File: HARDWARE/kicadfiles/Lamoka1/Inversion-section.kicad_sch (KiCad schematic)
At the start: 30 parts, among them Q1 NMOS, Q2 NMOS, Q3 CSD19536KCS, Q4 CSD19536KCS, Q5 CSD19536KCS, Q6 CSD19536KCS, U4 LM5122MH/NOPB

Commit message: Finishing routing for H bridge (Inversion-section)
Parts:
- added C22, C23: C, symbol Device:C
- added D11, D12: D, symbol Device:D
- added R10, R12: R, SOIC_14L_TEX, symbol Device:R
- added R13, R14, R15, R16: 10k, symbol Device:R
- added R17, R18: R, symbol Device:R
- added U5, U6: UCC27735DR, SOIC_14L_TEX, symbol UCC27735DR:UCC27735DR
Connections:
- net 11-14v input: now also D11.2 (A), D12.2 (A), U5.4 (EN/NC), U5.7 (VDD), U6.4 (EN/NC), U6.7 (VDD)
- net G4S: now also C23.2, R14.1, U6.11 (HS)
- net GND: now also R15.1, R16.1, U5.3 (VSS), U5.5 (COM), U6.3 (VSS), U6.5 (COM)
- net Q3G: now also R13.2, R17.2
- net Q3S: now also C22.2, R13.1, U5.11 (HS)
- net Q4G: now also R14.2, R18.2
- net Q5G: now also R10.1, R15.2
- net Q6G: now also R12.1, R16.2
- new net GPIO1: U5.1 (HI)
- new net GPIO2: U5.2 (LI)
- new net GPIO3: U6.1 (HI)
- new net GPIO4: U6.2 (LI)
- new net HB1: C22.1, D11.1 (K), U5.13 (HB)
- new net HB2: C23.1, D12.1 (K), U6.13 (HB)
- new net HO1: R17.1, U5.12 (HO)
- new net HO2: R18.1, U6.12 (HO)
- new net LO1: R10.2, U5.6 (LO)
- new net LO2: R12.2, U6.6 (LO)
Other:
- note removed: "Need the H bridge setup here"

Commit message: ADD logo, repo grade, and cosmetic/finishing H bridge connections
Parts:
- added J1: Connect to transformer, Connector:Tag-Connect_TC2030-IDC-FP_2x03_P1.27mm_Vertical, symbol Connector:Conn_01x02_Pin
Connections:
- net G4S: now also J1.1 (Pin_1)
- net Q3S: now also J1.2 (Pin_2)
- net HO1: no longer names the net of R17.1, U5.12 (HO)
- net HO2: no longer names the net of R18.1, U6.12 (HO)
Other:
- note added: "H-Bridge-Sub-Section"
- note removed: "Then transformer here"
- moved on the sheet: C22, C23, D11, D12, Q3, Q4, Q5, Q6, R10, R12, R13, R14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

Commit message: Improving repository
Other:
- title: Inverting  -> Inversion-Section 
- moved on the sheet: C22, C23, D11, D12, J1, Q3, Q4, Q5, Q6, R10, R12, R13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

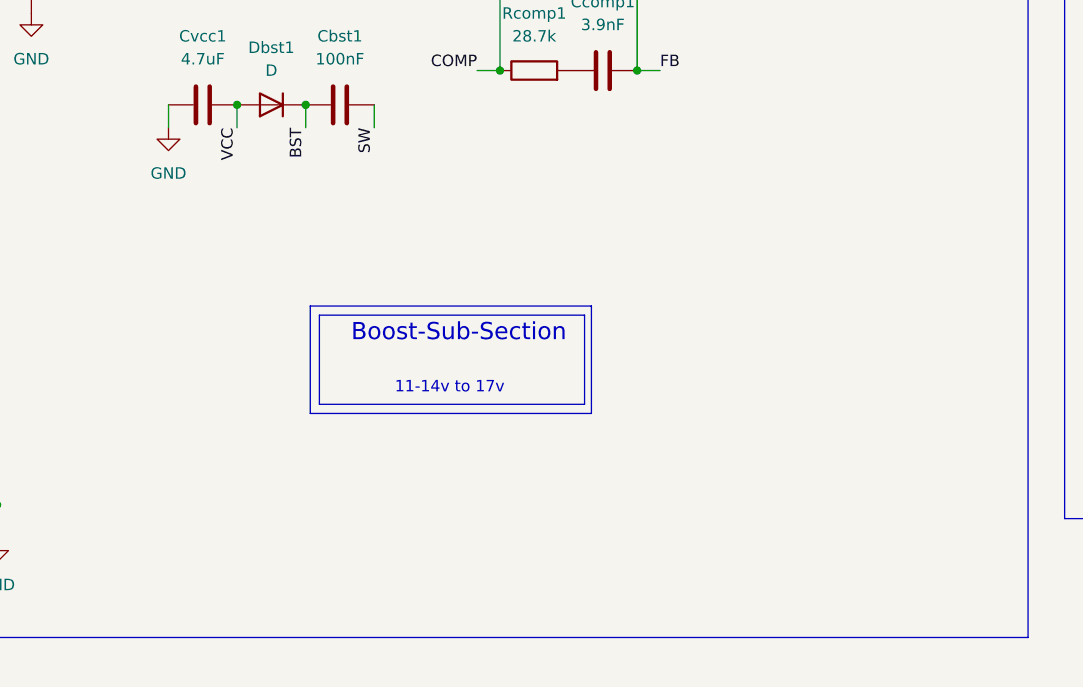
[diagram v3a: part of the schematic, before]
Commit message: ADD fan connection, and finish buck converter 5v
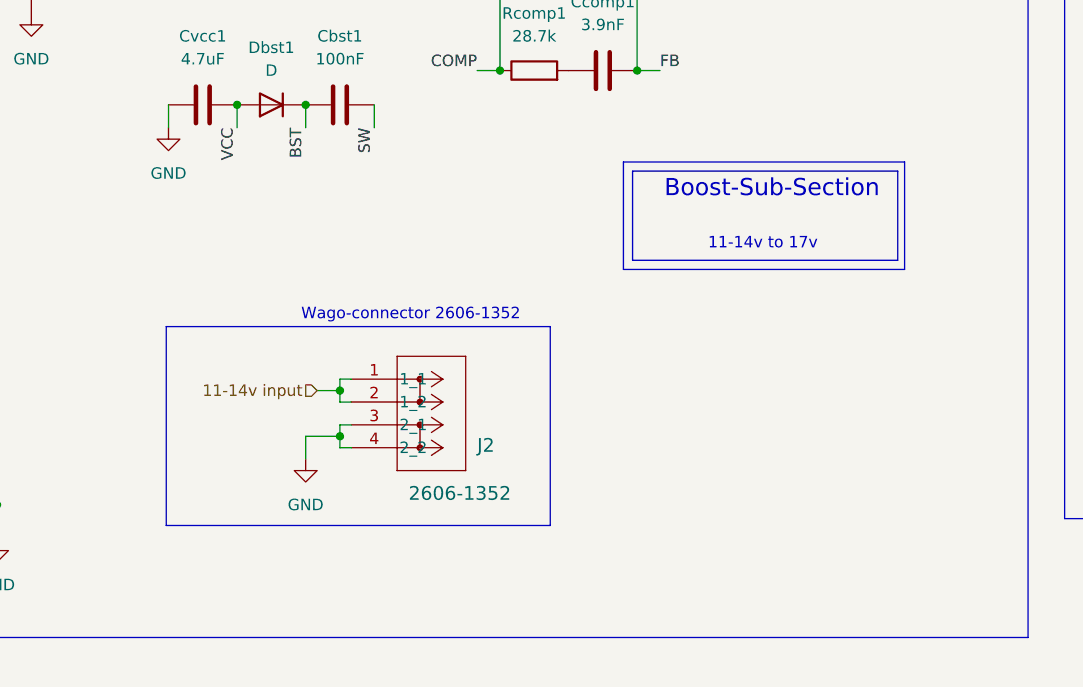
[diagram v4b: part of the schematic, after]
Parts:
- added J2: 2606-1352, CONN2_2606-1352_WAG, symbol Wago-connector:2606-1352
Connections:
- net 11-14v input: now also J2.1 (1_1), J2.2 (1_2)
- net GND: now also J2.3 (2_1), J2.4 (2_2)
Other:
- note added: "Wago-connector 2606-1352"

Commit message: ADD temp sensors, more doccumentation regarding design
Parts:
- added U9: TMP235A2DBZR, DBZ0003A-IPC_A, symbol TMP235A2DBZR:TMP235A2DBZR
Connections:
- net GND: now also U9.3 (GND)
- new net 3v3: U9.1 (VDD)
- new net TEMP_INV: U9.2 (VOUT)
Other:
- note added: "Temperature-Sensor"
